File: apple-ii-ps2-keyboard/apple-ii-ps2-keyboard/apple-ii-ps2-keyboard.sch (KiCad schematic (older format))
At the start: 23 parts, among them J1 PS/2, J2 apple-ii

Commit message: Add initial prototype PCB routing
I'll look at this tomorrow before I send it out for printing.
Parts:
- C1: footprint (none) -> Capacitor_THT:CP_Radial_D5.0mm_P2.50mm
- C2: footprint (none) -> Capacitor_THT:C_Disc_D3.8mm_W2.6mm_P2.50mm
- D2, D3: footprint (none) -> LED_THT:LED_D3.0mm
- R1, R10, R11, R12, R13, R14, R15, R2, R3, R4, R5, R6, R7, R8, R9: footprint (none) -> Resistor_THT:R_Axial_DIN0204_L3.6mm_D1.6mm_P5.08mm_Horizontal
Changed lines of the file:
@@
 F 0 "C1" H 6138 4646 50  0000 L CNN
 F 1 "100uF" H 6138 4555 50  0000 L CNN
-F 2 "" H 6050 4600 50  0001 C CNN
+F 2 "Capacitor_THT:CP_Radial_D5.0mm_P2.50mm" H 6050 4600 50  0001 C CNN
 F 3 "~" H 6050 4600 50  0001 C CNN
 	1    6050 4600
@@
 F 0 "C2" H 6542 4646 50  0000 L CNN
 F 1 "0.1uF" H 6542 4555 50  0000 L CNN
-F 2 "" H 6450 4600 50  0001 C CNN
+F 2 "Capacitor_THT:C_Disc_D3.8mm_W2.6mm_P2.50mm" H 6450 4600 50  0001 C CNN
 F 3 "~" H 6450 4600 50  0001 C CNN
 	1    6450 4600
@@
 F 0 "R2" V 5600 1500 50  0000 C CNN
 F 1 "47" V 5600 1800 50  0000 C CNN
-F 2 "" H 5650 1650 50  0001 C CNN
+F 2 "Resistor_THT:R_Axial_DIN0204_L3.6mm_D1.6mm_P5.08mm_Horizontal" H 5650 1650 50  0001 C CNN
 F 3 "~" H 5650 1650 50  0001 C CNN
 	1    5650 1650
@@
 F 0 "R3" V 5600 1600 50  0000 C CNN
 F 1 "47" V 5600 1900 50  0000 C CNN
-F 2 "" H 5650 1750 50  0001 C CNN
+F 2 "Resistor_THT:R_Axial_DIN0204_L3.6mm_D1.6mm_P5.08mm_Horizontal" H 5650 1750 50  0001 C CNN
 F 3 "~" H 5650 1750 50  0001 C CNN
 	1    5650 1750
@@
 F 0 "R4" V 5600 1800 50  0000 C CNN
 F 1 "47" V 5600 2100 50  0000 C CNN
-F 2 "" H 5650 1950 50  0001 C CNN
+F 2 "Resistor_THT:R_Axial_DIN0204_L3.6mm_D1.6mm_P5.08mm_Horizontal" H 5650 1950 50  0001 C CNN
 F 3 "~" H 5650 1950 50  0001 C CNN
 	1    5650 1950
@@
 F 0 "R5" V 5600 1900 50  0000 C CNN
 F 1 "47" V 5600 2200 50  0000 C CNN
-F 2 "" H 5650 2050 50  0001 C CNN
+F 2 "Resistor_THT:R_Axial_DIN0204_L3.6mm_D1.6mm_P5.08mm_Horizontal" H 5650 2050 50  0001 C CNN
 F 3 "~" H 5650 2050 50  0001 C CNN
 	1    5650 2050
@@
 F 0 "R6" V 5600 2000 50  0000 C CNN
 F 1 "47" V 5600 2300 50  0000 C CNN
-F 2 "" H 5650 2150 50  0001 C CNN
+F 2 "Resistor_THT:R_Axial_DIN0204_L3.6mm_D1.6mm_P5.08mm_Horizontal" H 5650 2150 50  0001 C CNN
 F 3 "~" H 5650 2150 50  0001 C CNN
 	1    5650 2150
@@
 F 0 "R10" V 7700 1900 50  0000 C CNN
 F 1 "47" V 7700 2200 50  0000 C CNN
-F 2 "" H 7750 2050 50  0001 C CNN
+F 2 "Resistor_THT:R_Axial_DIN0204_L3.6mm_D1.6mm_P5.08mm_Horizontal" H 7750 2050 50  0001 C CNN
 F 3 "~" H 7750 2050 50  0001 C CNN
 	1    7750 2050
@@
 F 0 "R11" V 7700 2000 50  0000 C CNN
 F 1 "47" V 7700 2300 50  0000 C CNN
-F 2 "" H 7750 2150 50  0001 C CNN
+F 2 "Resistor_THT:R_Axial_DIN0204_L3.6mm_D1.6mm_P5.08mm_Horizontal" H 7750 2150 50  0001 C CNN
 F 3 "~" H 7750 2150 50  0001 C CNN
 	1    7750 2150
@@
 F 0 "R12" V 5654 3050 50  0000 C CNN
 F 1 "47" V 5745 3050 50  0000 C CNN
-F 2 "" H 5850 3050 50  0001 C CNN
+F 2 "Resistor_THT:R_Axial_DIN0204_L3.6mm_D1.6mm_P5.08mm_Horizontal" H 5850 3050 50  0001 C CNN
 F 3 "~" H 5850 3050 50  0001 C CNN
 	1    5850 3050
@@
 F 0 "R13" V 5654 3450 50  0000 C CNN
 F 1 "47" V 5745 3450 50  0000 C CNN
-F 2 "" H 5850 3450 50  0001 C CNN
+F 2 "Resistor_THT:R_Axial_DIN0204_L3.6mm_D1.6mm_P5.08mm_Horizontal" H 5850 3450 50  0001 C CNN
 F 3 "~" H 5850 3450 50  0001 C CNN
 	1    5850 3450
@@
 F 0 "R1" H 5959 1396 50  0000 L CNN
 F 1 "4.7K" H 5959 1305 50  0000 L CNN
-F 2 "" H 5900 1350 50  0001 C CNN
+F 2 "Resistor_THT:R_Axial_DIN0204_L3.6mm_D1.6mm_P5.08mm_Horizontal" H 5900 1350 50  0001 C CNN
 F 3 "~" H 5900 1350 50  0001 C CNN
 	1    5900 1350
@@
 F 0 "R7" H 6009 2346 50  0000 L CNN
 F 1 "1K" H 6009 2255 50  0000 L CNN
-F 2 "" H 5950 2300 50  0001 C CNN
+F 2 "Resistor_THT:R_Axial_DIN0204_L3.6mm_D1.6mm_P5.08mm_Horizontal" H 5950 2300 50  0001 C CNN
 F 3 "~" H 5950 2300 50  0001 C CNN
 	1    5950 2300
@@
 F 0 "R9" V 7700 1800 50  0000 C CNN
 F 1 "47" V 7700 2100 50  0000 C CNN
-F 2 "" H 7750 1950 50  0001 C CNN
+F 2 "Resistor_THT:R_Axial_DIN0204_L3.6mm_D1.6mm_P5.08mm_Horizontal" H 7750 1950 50  0001 C CNN
 F 3 "~" H 7750 1950 50  0001 C CNN
 	1    7750 1950
@@
 F 0 "R8" V 7700 1700 50  0000 C CNN
 F 1 "47" V 7700 2000 50  0000 C CNN
-F 2 "" H 7750 1850 50  0001 C CNN
+F 2 "Resistor_THT:R_Axial_DIN0204_L3.6mm_D1.6mm_P5.08mm_Horizontal" H 7750 1850 50  0001 C CNN
 F 3 "~" H 7750 1850 50  0001 C CNN
 	1    7750 1850
@@
 F 0 "D2" V 6089 5632 50  0000 R CNN
 F 1 "LED" V 5998 5632 50  0000 R CNN
-F 2 "" H 6050 5750 50  0001 C CNN
+F 2 "LED_THT:LED_D3.0mm" H 6050 5750 50  0001 C CNN
 F 3 "~" H 6050 5750 50  0001 C CNN
 	1    6050 5750
@@
 F 0 "D3" V 6439 5632 50  0000 R CNN
 F 1 "LED" V 6348 5632 50  0000 R CNN
-F 2 "" H 6400 5750 50  0001 C CNN
+F 2 "LED_THT:LED_D3.0mm" H 6400 5750 50  0001 C CNN
 F 3 "~" H 6400 5750 50  0001 C CNN
 	1    6400 5750
@@
 F 0 "R14" H 6109 5546 50  0000 L CNN
 F 1 "1K" H 6109 5455 50  0000 L CNN
-F 2 "" H 6050 5500 50  0001 C CNN
+F 2 "Resistor_THT:R_Axial_DIN0204_L3.6mm_D1.6mm_P5.08mm_Horizontal" H 6050 5500 50  0001 C CNN
 F 3 "~" H 6050 5500 50  0001 C CNN
 	1    6050 5500
@@
 F 0 "R15" H 6459 5546 50  0000 L CNN
 F 1 "1K" H 6459 5455 50  0000 L CNN
-F 2 "" H 6400 5500 50  0001 C CNN
+F 2 "Resistor_THT:R_Axial_DIN0204_L3.6mm_D1.6mm_P5.08mm_Horizontal" H 6400 5500 50  0001 C CNN
 F 3 "~" H 6400 5500 50  0001 C CNN
 	1    6400 5500
@@
 $EndComp
 $Comp
-L power:GND #PWR?
+L power:GND #PWR0101
 U 1 1 611FD95A
 P 6050 5900
-F 0 "#PWR?" H 6050 5650 50  0001 C CNN
+F 0 "#PWR0101" H 6050 5650 50  0001 C CNN
 F 1 "GND" H 6055 5727 50  0000 C CNN
 F 2 "" H 6050 5900 50  0001 C CNN
@@
 $EndComp
 $Comp
-L power:GND #PWR?
+L power:GND #PWR0102
 U 1 1 611FDFFC
 P 6400 5900
-F 0 "#PWR?" H 6400 5650 50  0001 C CNN
+F 0 "#PWR0102" H 6400 5650 50  0001 C CNN
 F 1 "GND" H 6405 5727 50  0000 C CNN
 F 2 "" H 6400 5900 50  0001 C CNN
@@
 APPLE_5V
 $Comp
-L power:VCC #PWR?
+L power:VCC #PWR0103
 U 1 1 611FF1B2
 P 6050 5400
-F 0 "#PWR?" H 6050 5250 50  0001 C CNN
+F 0 "#PWR0103" H 6050 5250 50  0001 C CNN
 F 1 "VCC" H 6065 5573 50  0000 C CNN
 F 2 "" H 6050 5400 50  0001 C CNN

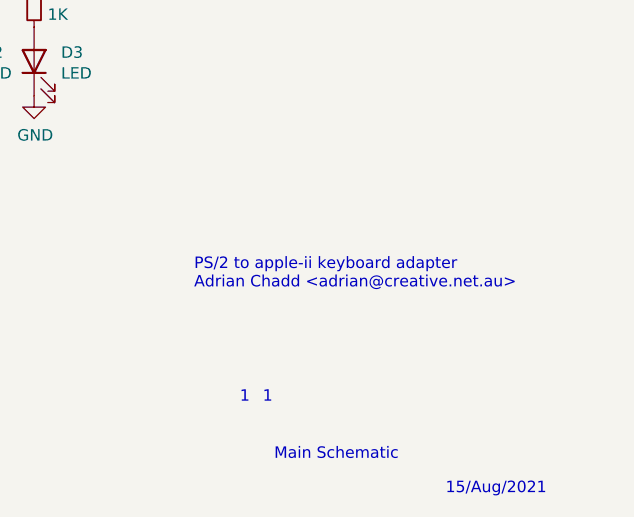
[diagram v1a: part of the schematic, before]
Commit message: Update the description to say prototype
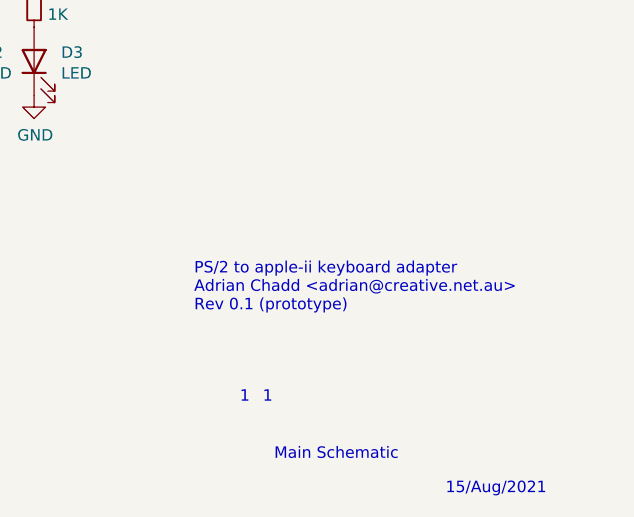
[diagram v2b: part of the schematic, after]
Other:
- note added: "PS/2 to apple-ii keyboard adapter\nAdrian Chadd <adrian@creative.net.au>\nRev 0.1 (prototype)"
- note removed: "PS/2 to apple-ii keyboard adapter\nAdrian Chadd <adrian@creative.net.au>"
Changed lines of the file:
@@
 Text Notes 8200 7650 0    50   ~ 0
 15/Aug/2021
-Text Notes 7100 6750 0    50   ~ 0
-PS/2 to apple-ii keyboard adapter\nAdrian Chadd <adrian@creative.net.au>
+Text Notes 7100 6850 0    50   ~ 0
+PS/2 to apple-ii keyboard adapter\nAdrian Chadd <adrian@creative.net.au>\nRev 0.1 (prototype)
 Text Notes 7300 7250 0    50   ~ 0
 1

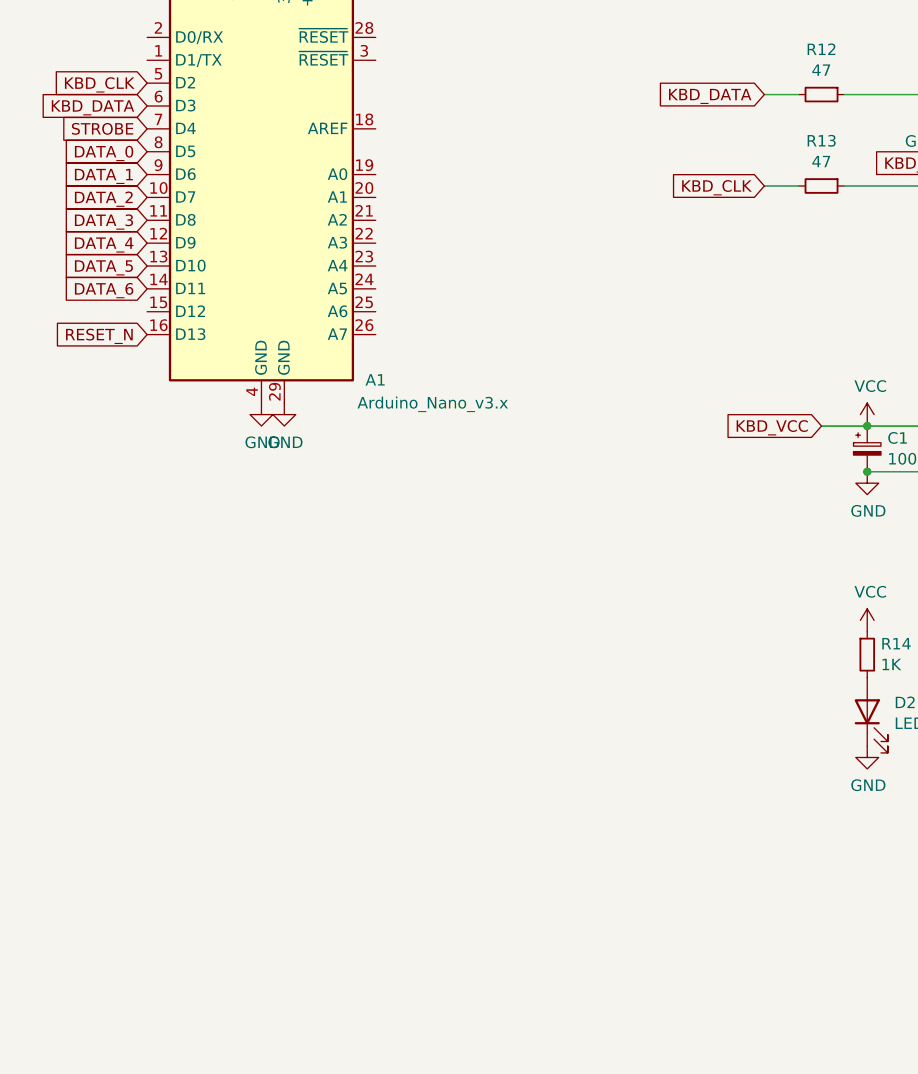
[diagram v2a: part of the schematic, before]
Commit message: * add shift button IO control for later * add the A0-A7 and power pins as expansion headers if I want to do   anything else
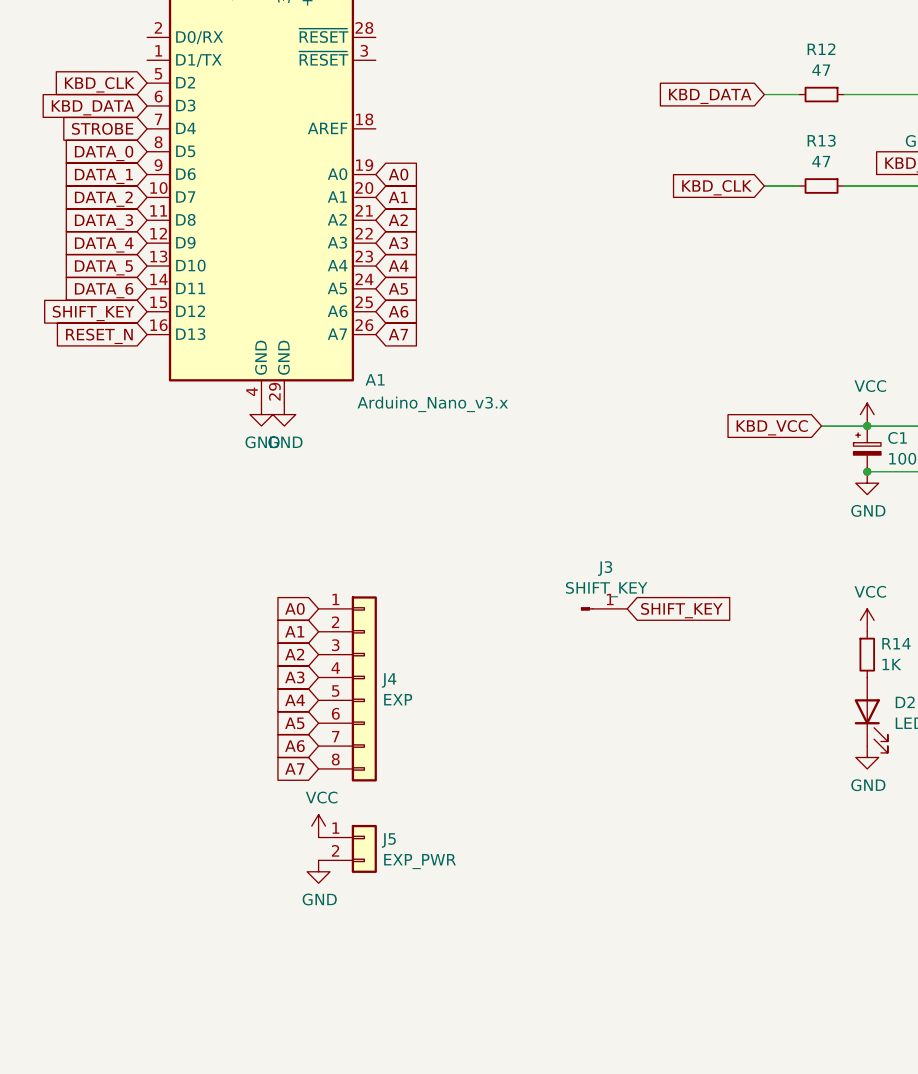
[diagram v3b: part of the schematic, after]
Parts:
- added J3: SHIFT_KEY, Connector_PinHeader_2.54mm:PinHeader_1x01_P2.54mm_Vertical, symbol Connector:Conn_01x01_Male
- added J4: EXP, Connector_PinHeader_2.54mm:PinHeader_1x08_P2.54mm_Vertical, symbol Connector_Generic:Conn_01x08
- added J5: EXP_PWR, Connector_PinHeader_2.54mm:PinHeader_1x02_P2.54mm_Vertical, symbol Connector_Generic:Conn_01x02
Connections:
- net GND: now also J5.2 (Pin_2)
- net VCC: now also J5.1 (Pin_1)
- net SHIFT_KEY: now reaches A1.15 (D12)
- net SHIFT_KEY: now also J3.1 (Pin_1)
- net A0: now reaches A1.19 (A0)
- net A0: now also J4.1 (Pin_1)
- net A1: now reaches A1.20 (A1)
- net A1: now also J4.2 (Pin_2)
- net A2: now reaches A1.21 (A2)
- net A2: now also J4.3 (Pin_3)
- net A3: now reaches A1.22 (A3)
- net A3: now also J4.4 (Pin_4)
- net A4: now reaches A1.23 (A4)
- net A4: now also J4.5 (Pin_5)
- net A5: now reaches A1.24 (A5)
- net A5: now also J4.6 (Pin_6)
- net A6: now reaches A1.25 (A6)
- net A6: now also J4.7 (Pin_7)
- net A7: now reaches A1.26 (A7)
- net A7: now also J4.8 (Pin_8)
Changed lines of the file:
@@
 Text Notes 7400 7250 0    50   ~ 0
 1
+$Comp
+L Connector:Conn_01x01_Male J3
+U 1 1 61261EA4
+P 4800 5300
+F 0 "J3" H 4908 5481 50  0000 C CNN
+F 1 "SHIFT_KEY" H 4908 5390 50  0000 C CNN
+F 2 "Connector_PinHeader_2.54mm:PinHeader_1x01_P2.54mm_Vertical" H 4800 5300 50  0001 C CNN
+F 3 "~" H 4800 5300 50  0001 C CNN
+	1    4800 5300
+	1    0    0    -1
+$EndComp
+Text GLabel 5000 5300 2    50   Input ~ 0
+SHIFT_KEY
+Text GLabel 2900 4000 0    50   Input ~ 0
+SHIFT_KEY
+$Comp
+L Connector_Generic:Conn_01x08 J4
+U 1 1 61263F5E
+P 3850 5600
+F 0 "J4" H 3930 5592 50  0000 L CNN
+F 1 "EXP" H 3930 5501 50  0000 L CNN
+F 2 "Connector_PinHeader_2.54mm:PinHeader_1x08_P2.54mm_Vertical" H 3850 5600 50  0001 C CNN
+F 3 "~" H 3850 5600 50  0001 C CNN
+	1    3850 5600
+	1    0    0    -1
+$EndComp
+Text GLabel 3650 5300 0    50   Input ~ 0
+A0
+Text GLabel 3650 5400 0    50   Input ~ 0
+A1
+Text GLabel 3650 5500 0    50   Input ~ 0
+A2
+Text GLabel 3650 5600 0    50   Input ~ 0
+A3
+Text GLabel 3650 5700 0    50   Input ~ 0
+A4
+Text GLabel 3650 5800 0    50   Input ~ 0
+A5
+Text GLabel 3650 5900 0    50   Input ~ 0
+A6
+Text GLabel 3650 6000 0    50   Input ~ 0
+A7
+$Comp
+L Connector_Generic:Conn_01x02 J5
+U 1 1 6126BACA
+P 3850 6300
+F 0 "J5" H 3930 6292 50  0000 L CNN
+F 1 "EXP_PWR" H 3930 6201 50  0000 L CNN
+F 2 "Connector_PinHeader_2.54mm:PinHeader_1x02_P2.54mm_Vertical" H 3850 6300 50  0001 C CNN
+F 3 "~" H 3850 6300 50  0001 C CNN
+	1    3850 6300
+	1    0    0    -1
+$EndComp
+$Comp
+L power:VCC #PWR0104
+U 1 1 6126C911
+P 3650 6300
+F 0 "#PWR0104" H 3650 6150 50  0001 C CNN
+F 1 "VCC" H 3665 6473 50  0000 C CNN
+F 2 "" H 3650 6300 50  0001 C CNN
+F 3 "" H 3650 6300 50  0001 C CNN
+	1    3650 6300
+	1    0    0    -1
+$EndComp
+$Comp
+L power:GND #PWR0105
+U 1 1 6126CCC6
+P 3650 6400
+F 0 "#PWR0105" H 3650 6150 50  0001 C CNN
+F 1 "GND" H 3655 6227 50  0000 C CNN
+F 2 "" H 3650 6400 50  0001 C CNN
+F 3 "" H 3650 6400 50  0001 C CNN
+	1    3650 6400
+	1    0    0    -1
+$EndComp
+Text GLabel 3900 3400 2    50   Input ~ 0
+A0
+Text GLabel 3900 3500 2    50   Input ~ 0
+A1
+Text GLabel 3900 3600 2    50   Input ~ 0
+A2
+Text GLabel 3900 3700 2    50   Input ~ 0
+A3
+Text GLabel 3900 3800 2    50   Input ~ 0
+A4
+Text GLabel 3900 3900 2    50   Input ~ 0
+A5
+Text GLabel 3900 4000 2    50   Input ~ 0
+A6
+Text GLabel 3900 4100 2    50   Input ~ 0
+A7
 $EndSCHEMATC
